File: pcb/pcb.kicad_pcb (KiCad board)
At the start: 4 copper layers, 170.2 x 137.2 mm, 173 parts, among them J1 Barrel_Jack, J10 Screw_Terminal_01x08, J11 Conn_01x08_Male, J12 Conn_01x08_Male, J13 Conn_01x08_Male, J14 Conn_01x08_Male, J15 Conn_01x02_Male, J2 Barrel_Jack, J3 Screw_Terminal_01x02, J4 Screw_Terminal_01x02, J5 Conn_02x05_Odd_Even, J6 Conn_01x06_Male, J7 Screw_Terminal_01x08, J8 Screw_Terminal_01x08, J9 Screw_Terminal_01x08, SW1 SW_SPDT, SW2 SW_SPDT, U1 CPC5001G, U10 LTV-847, U11 LTV-847, U12 MCP23017-E_SP, U13 MCP23017-E_SP, U2 MCP23017-E_SP, U3 LTV-847, U4 LTV-847, U5 LTV-847, U6 LTV-847, U7 MCP23017-E_SP, U8 LTV-847, U9 LTV-847

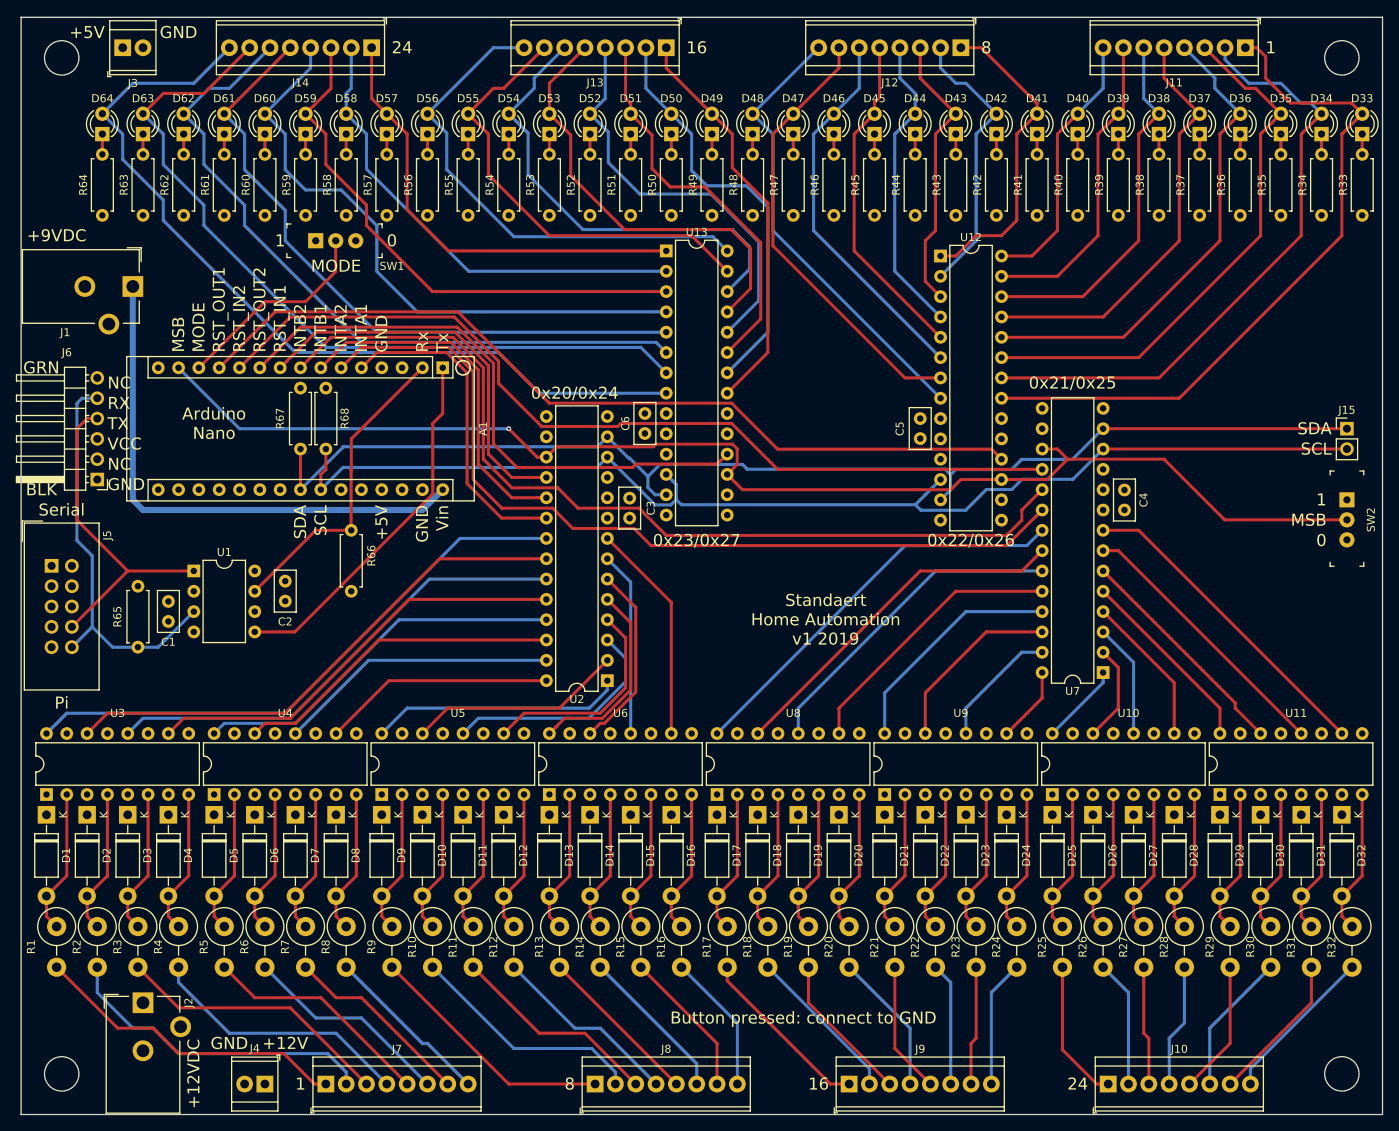
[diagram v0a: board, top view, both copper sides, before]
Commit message: Changed some footprints, spacing out components
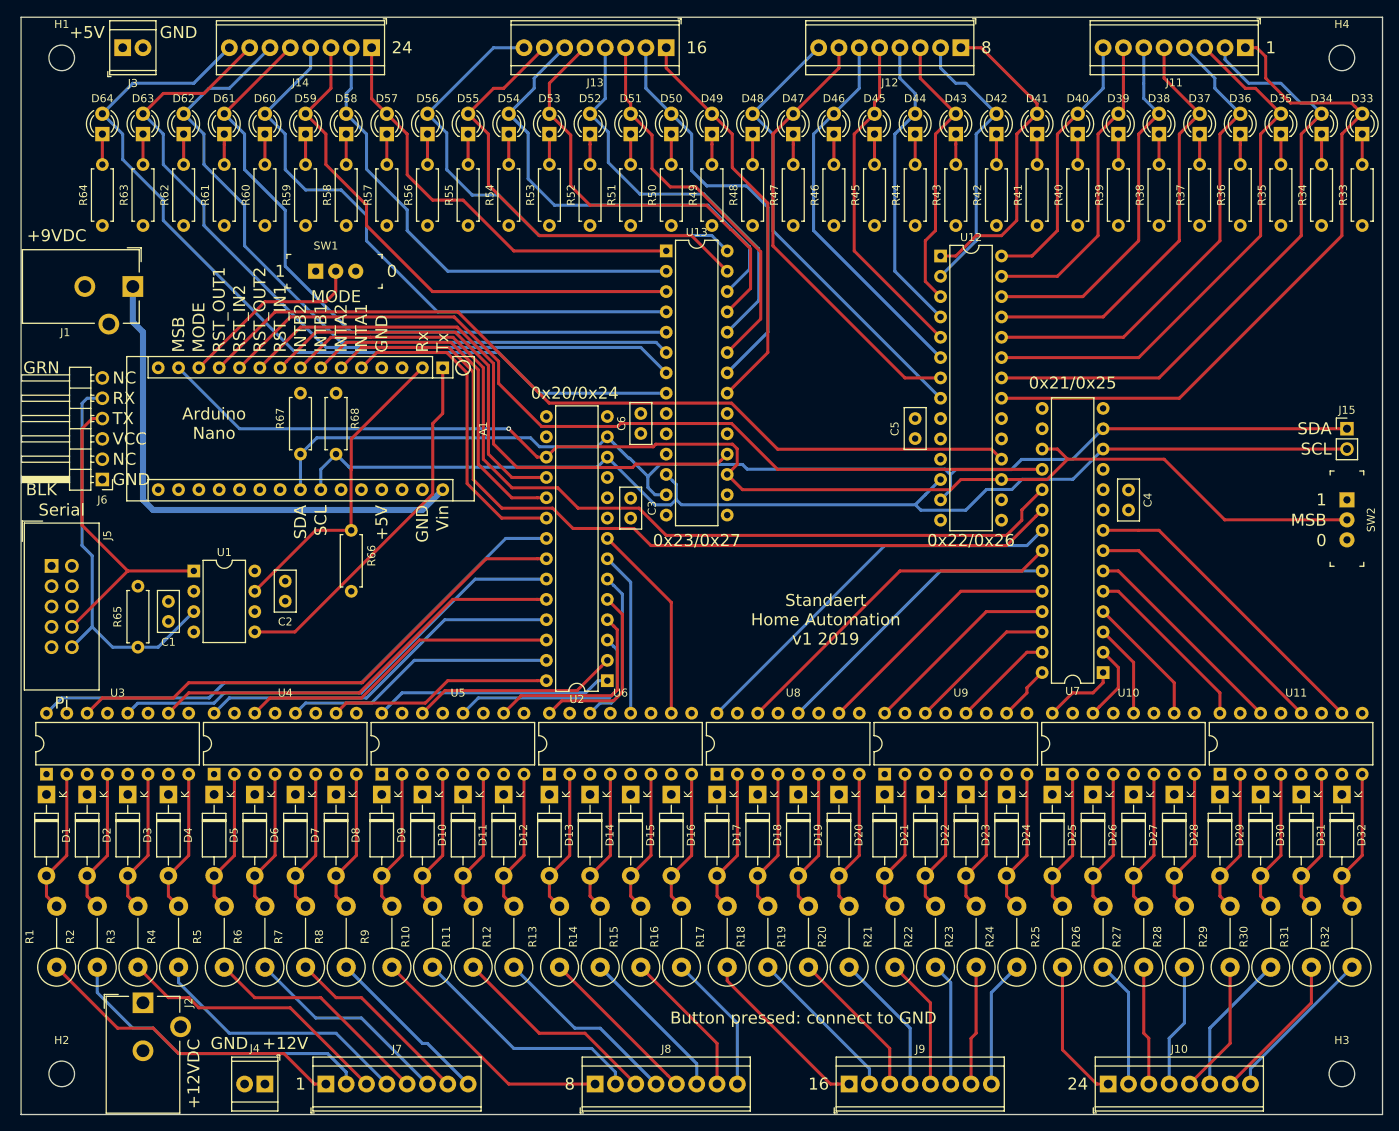
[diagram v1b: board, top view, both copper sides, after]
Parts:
- H1, H2, H3, H4: footprint MountingHole:MountingHole_4.3mm_M4 -> MountingHole:MountingHole_3.2mm_M3
- R1, R10, R11, R12, R13, R14, R15, R16, R17, R18, R19, R2, R20, R21, R22, R23, R24, R25, R26, R27, R28, R29, R3, R30, R31, R32, R4, R5, R6, R7, R8, R9: footprint Resistor_THT:R_Axial_DIN0414_L11.9mm_D4.5mm_P5.08mm_Vertical -> Resistor_THT:R_Axial_DIN0414_L11.9mm_D4.5mm_P7.62mm_Vertical
- moved R1 5.08 mm to (88.3, 139.1), turned to 90 degrees
- moved R10 5.08 mm to (135.3, 139.1), turned to 90 degrees
- moved R11 5.08 mm to (140.3, 139.1), turned to 90 degrees
- moved R12 5.08 mm to (145.4, 139.1), turned to 90 degrees
- moved R13 5.08 mm to (151.1, 139.1), turned to 90 degrees
- moved R14 5.08 mm to (156.2, 139.1), turned to 90 degrees
- moved R15 5.08 mm to (161.3, 139.1), turned to 90 degrees
- moved R16 5.08 mm to (166.4, 139.1), turned to 90 degrees
- moved R17 5.08 mm to (172.1, 139.1), turned to 90 degrees
- moved R18 5.08 mm to (177.2, 139.1), turned to 90 degrees
- moved R19 5.08 mm to (182.2, 139.1), turned to 90 degrees
- moved R2 5.08 mm to (93.3, 139.1), turned to 90 degrees
- moved R20 5.08 mm to (187.3, 139.1), turned to 90 degrees
- moved R21 5.08 mm to (193.0, 139.1), turned to 90 degrees
- moved R22 5.08 mm to (198.1, 139.1), turned to 90 degrees
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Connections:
- R1 pad 1: Net-(D1-Pad2) -> /Input 1/Pin0
- R1 pad 2: /Input 1/Pin0 -> Net-(D1-Pad2)
- R10 pad 1: Net-(D10-Pad2) -> /Input 1/Pin9
- R10 pad 2: /Input 1/Pin9 -> Net-(D10-Pad2)
- R11 pad 1: Net-(D11-Pad2) -> /Input 1/Pin10
- R11 pad 2: /Input 1/Pin10 -> Net-(D11-Pad2)
- R12 pad 1: Net-(D12-Pad2) -> /Input 1/Pin11
- R12 pad 2: /Input 1/Pin11 -> Net-(D12-Pad2)
- R13 pad 1: Net-(D13-Pad2) -> /Input 1/Pin12
- R13 pad 2: /Input 1/Pin12 -> Net-(D13-Pad2)
- R14 pad 1: Net-(D14-Pad2) -> /Input 1/Pin13
- R14 pad 2: /Input 1/Pin13 -> Net-(D14-Pad2)
- R15 pad 1: Net-(D15-Pad2) -> /Input 1/Pin14
- R15 pad 2: /Input 1/Pin14 -> Net-(D15-Pad2)
- R16 pad 1: Net-(D16-Pad2) -> /Input 1/Pin15
- R16 pad 2: /Input 1/Pin15 -> Net-(D16-Pad2)
- R17 pad 1: Net-(D17-Pad2) -> /Input 2/Pin0
- R17 pad 2: /Input 2/Pin0 -> Net-(D17-Pad2)
- R18 pad 1: Net-(D18-Pad2) -> /Input 2/Pin1
- R18 pad 2: /Input 2/Pin1 -> Net-(D18-Pad2)
- R19 pad 1: Net-(D19-Pad2) -> /Input 2/Pin2
- R19 pad 2: /Input 2/Pin2 -> Net-(D19-Pad2)
- R2 pad 1: Net-(D2-Pad2) -> /Input 1/Pin1
- R2 pad 2: /Input 1/Pin1 -> Net-(D2-Pad2)
- R20 pad 1: Net-(D20-Pad2) -> /Input 2/Pin3
- R20 pad 2: /Input 2/Pin3 -> Net-(D20-Pad2)
- R21 pad 1: Net-(D21-Pad2) -> /Input 2/Pin4
- R21 pad 2: /Input 2/Pin4 -> Net-(D21-Pad2)
- R22 pad 1: Net-(D22-Pad2) -> /Input 2/Pin5
- R22 pad 2: /Input 2/Pin5 -> Net-(D22-Pad2)
- R23 pad 1: Net-(D23-Pad2) -> /Input 2/Pin6
- R23 pad 2: /Input 2/Pin6 -> Net-(D23-Pad2)
- R24 pad 1: Net-(D24-Pad2) -> /Input 2/Pin7
- R24 pad 2: /Input 2/Pin7 -> Net-(D24-Pad2)
- R25 pad 1: Net-(D25-Pad2) -> /Input 2/Pin8
- R25 pad 2: /Input 2/Pin8 -> Net-(D25-Pad2)
- R26 pad 1: Net-(D26-Pad2) -> /Input 2/Pin9
- R26 pad 2: /Input 2/Pin9 -> Net-(D26-Pad2)
- R27 pad 1: Net-(D27-Pad2) -> /Input 2/Pin10
- R27 pad 2: /Input 2/Pin10 -> Net-(D27-Pad2)
- R28 pad 1: Net-(D28-Pad2) -> /Input 2/Pin11
- R28 pad 2: /Input 2/Pin11 -> Net-(D28-Pad2)
- R29 pad 1: Net-(D29-Pad2) -> /Input 2/Pin12
- R29 pad 2: /Input 2/Pin12 -> Net-(D29-Pad2)
- R3 pad 1: Net-(D3-Pad2) -> /Input 1/Pin2
- R3 pad 2: /Input 1/Pin2 -> Net-(D3-Pad2)
- R30 pad 1: Net-(D30-Pad2) -> /Input 2/Pin13
- R30 pad 2: /Input 2/Pin13 -> Net-(D30-Pad2)
- R31 pad 1: Net-(D31-Pad2) -> /Input 2/Pin14
- R31 pad 2: /Input 2/Pin14 -> Net-(D31-Pad2)
- R32 pad 1: Net-(D32-Pad2) -> /Input 2/Pin15
- R32 pad 2: /Input 2/Pin15 -> Net-(D32-Pad2)
- R4 pad 1: Net-(D4-Pad2) -> /Input 1/Pin3
- R4 pad 2: /Input 1/Pin3 -> Net-(D4-Pad2)
- R5 pad 1: Net-(D5-Pad2) -> /Input 1/Pin4
- R5 pad 2: /Input 1/Pin4 -> Net-(D5-Pad2)
- R6 pad 1: Net-(D6-Pad2) -> /Input 1/Pin5
- R6 pad 2: /Input 1/Pin5 -> Net-(D6-Pad2)
- R7 pad 1: Net-(D7-Pad2) -> /Input 1/Pin6
- R7 pad 2: /Input 1/Pin6 -> Net-(D7-Pad2)
- R8 pad 1: Net-(D8-Pad2) -> /Input 1/Pin7
- R8 pad 2: /Input 1/Pin7 -> Net-(D8-Pad2)
- R9 pad 1: Net-(D9-Pad2) -> /Input 1/Pin8
- R9 pad 2: /Input 1/Pin8 -> Net-(D9-Pad2)
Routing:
- net /Input 2/IN5: track 22.8 -> 18.8 mm
- net /Input 2/IN4: track 29.0 -> 24.9 mm
- net /Input 1/IN13: track 23.5 -> 20.0 mm
- net /Input 2/IN6: track 15.6 -> 12.7 mm
- net /Input 2/IN2: track 40.8 -> 37.8 mm
- net /Input 2/IN3: track 34.6 -> 31.7 mm
- net /Output 2/Out8: track 56.6 -> 54.0 mm
- net /Input 2/IN9: track 12.3 -> 9.72 mm
- net /Input 2/IN11: track 18.9 -> 16.4 mm
- net /Input 2/IN10: track 14.3 -> 11.7 mm
- net /Input 1/IN15: track 27.7 -> 25.2 mm
- net /Input 1/IN14: track 23.1 -> 20.5 mm
- net /Input 2/IN7: track 9.46 -> 6.92 mm
- net SCL: track 149.9 -> 147.4 mm
- net /Input 1/IN12: track 24.9 -> 22.6 mm
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
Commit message: Silkscreen tweaks etc.
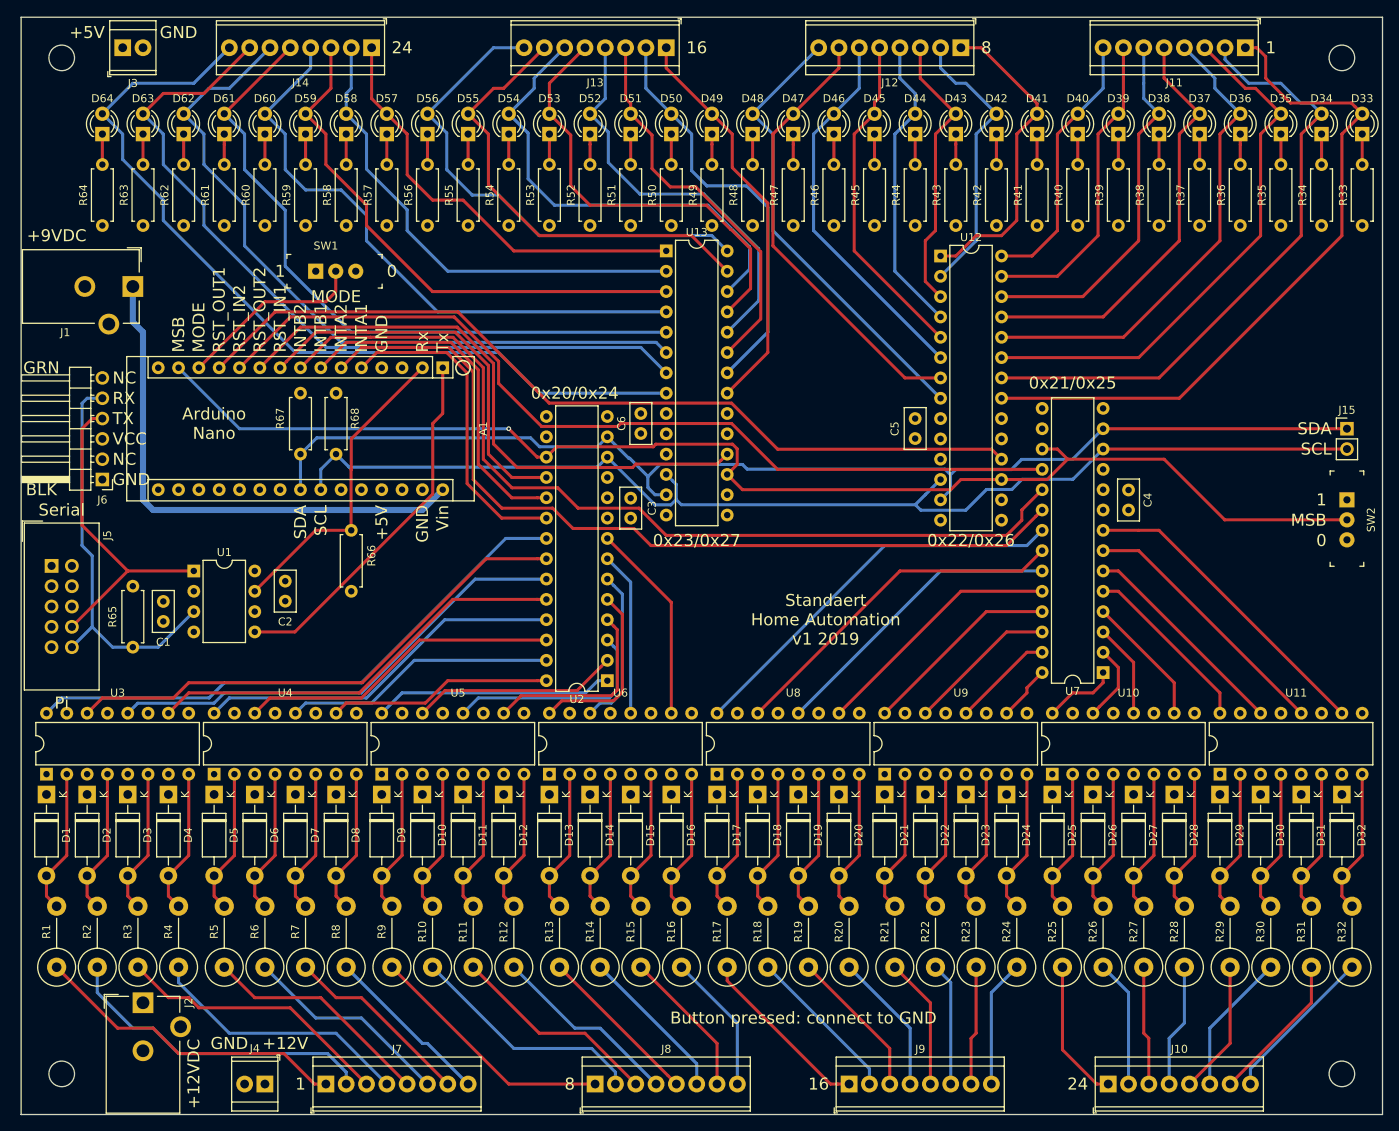
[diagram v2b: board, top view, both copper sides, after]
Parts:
- moved C1 0.64 mm to (101.6, 93.3)
- moved R65 0.63 mm to (97.8, 91.4)

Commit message: Some traces done
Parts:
- moved R10 1.80 mm to (136.5, 137.8)
- moved R12 1.80 mm to (146.7, 137.8)
- moved R13 1.80 mm to (152.4, 137.8)
- moved R15 1.80 mm to (162.6, 137.8)
- moved R18 1.80 mm to (178.4, 137.8)
- moved R20 1.80 mm to (188.6, 137.8)
- moved R21 1.80 mm to (194.3, 137.8)
- moved R23 1.80 mm to (204.5, 137.8)
- moved R24 1.80 mm to (209.6, 137.8)
- moved R26 1.80 mm to (220.3, 137.8)
- moved R27 1.80 mm to (225.4, 137.8)
- moved R29 1.80 mm to (236.2, 137.8)
- moved R30 1.80 mm to (241.3, 137.8)
- moved R32 1.80 mm to (251.5, 137.8)
- moved R4 1.80 mm to (104.8, 137.8)
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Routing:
- net +12V: track 0.00 -> 81.3 mm
- net /Input 2/Pin15: track 19.9 -> 23.1 mm
- net /Input 2/Pin0: track 22.3 -> 24.3 mm
- net /Input 2/Pin6: track 14.9 -> 16.7 mm
- net /Input 2/Pin7: track 15.9 -> 17.7 mm
- net /Input 2/Pin13: track 17.8 -> 19.6 mm
- net /Input 2/Pin12: track 16.7 -> 18.5 mm
- net /Input 2/Pin11: track 15.4 -> 17.2 mm
- net /Input 2/Pin14: track 18.8 -> 20.6 mm
- net /Input 2/Pin8: track 17.8 -> 19.2 mm
- net /Input 2/Pin10: track 14.9 -> 16.1 mm
- net /Input 1/Pin15: track 17.5 -> 18.2 mm
- net /Input 2/Pin2: track 18.8 -> 19.6 mm
- net /Input 2/Pin5: track 15.4 -> 16.1 mm
- net /Input 1/Pin2: track 34.6 -> 35.4 mm
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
